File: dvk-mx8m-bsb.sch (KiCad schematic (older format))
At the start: 12 parts, among them J101 IMX8M-SOM, J102 TEST_1P

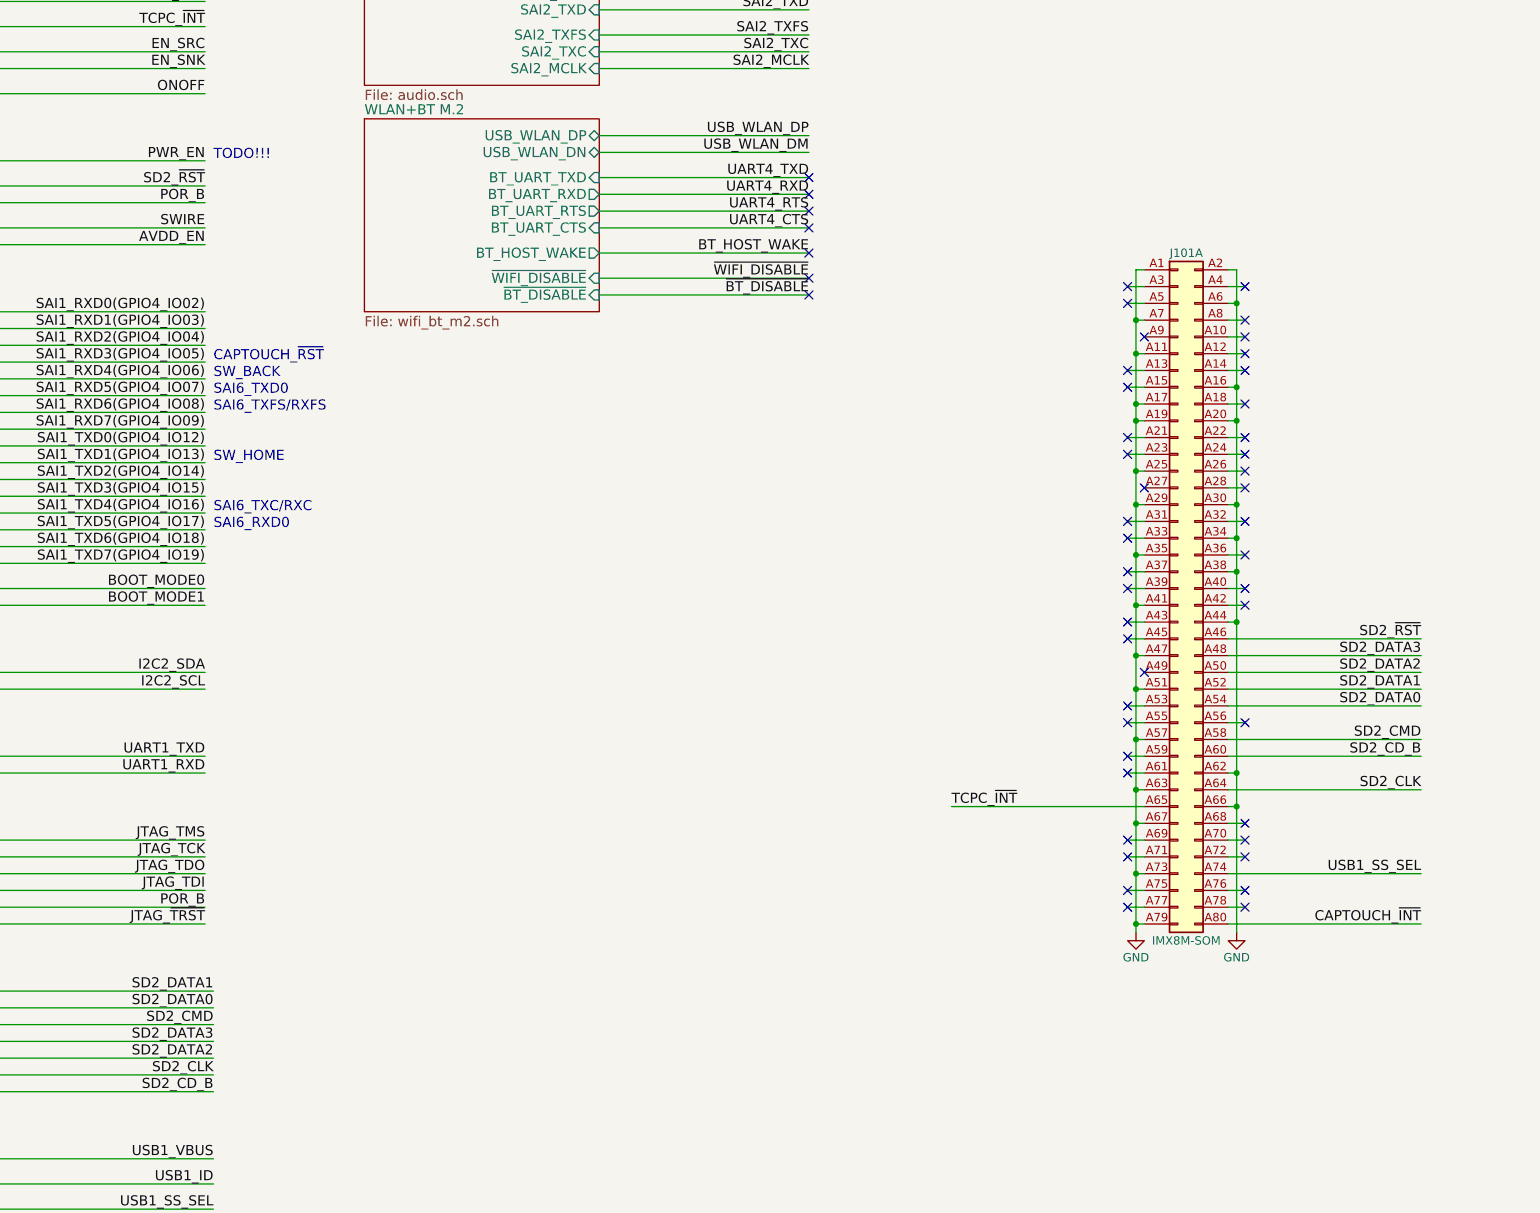
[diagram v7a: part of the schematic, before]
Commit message: Add demultiplexer to uSDHC2 for the uSD and WiFi's SDIO interfaces, include the DEMUX's (TS3A27518E) 24QFN footprint
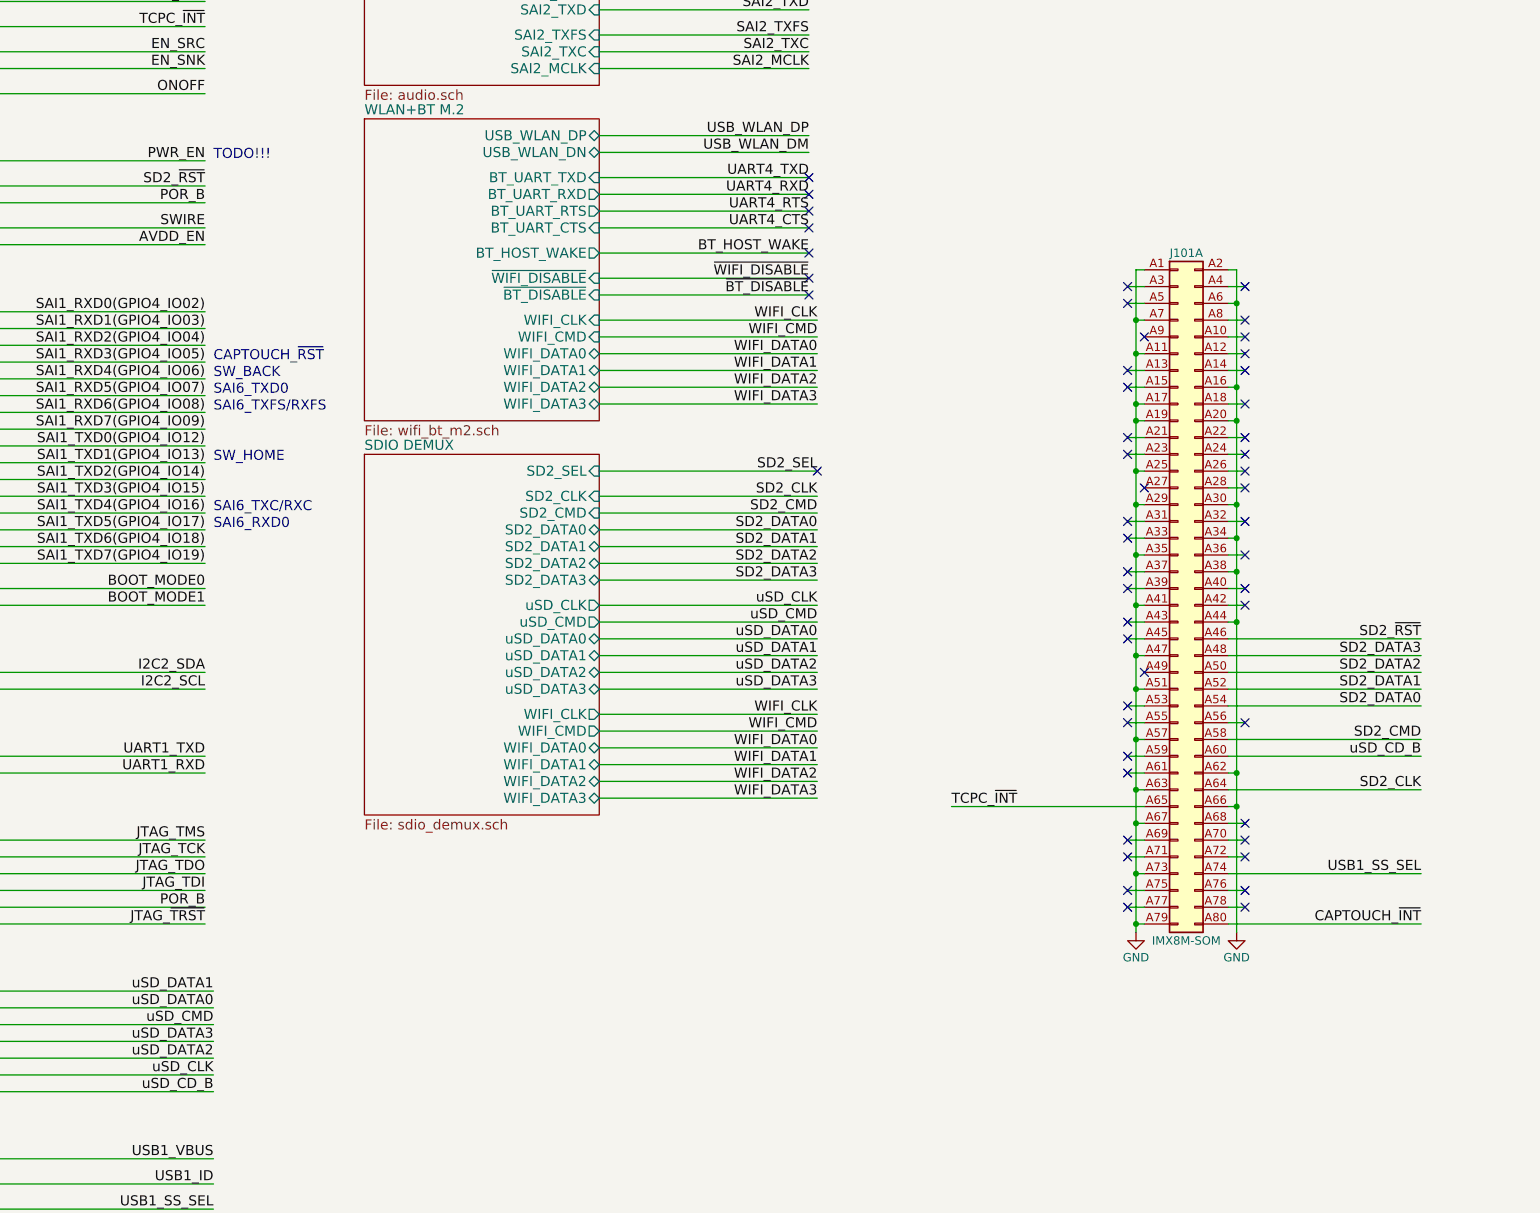
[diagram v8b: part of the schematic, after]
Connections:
- net SD2_CD_B renamed uSD_CD_B
- no-connect marks 130 -> 131
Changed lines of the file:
@@
 $Descr A2 23386 16535
 encoding utf-8
-Sheet 1 15
+Sheet 1 16
 Title "DVK-MX8M-BSB"
 Date "2018-05-02"
@@
 GPIO1_IO13
 Text Label 3250 6700 2    60   ~ 0
-SD2_DATA1
+uSD_DATA1
 Text Label 3250 6800 2    60   ~ 0
-SD2_DATA0
+uSD_DATA0
 Text Label 3250 6900 2    60   ~ 0
-SD2_CMD
+uSD_CMD
 Text Label 3250 7000 2    60   ~ 0
-SD2_DATA3
+uSD_DATA3
 Text Label 3250 7100 2    60   ~ 0
-SD2_DATA2
+uSD_DATA2
 Text Label 3250 7200 2    60   ~ 0
-SD2_CLK
+uSD_CLK
 Text Label 3250 7300 2    60   ~ 0
-SD2_CD_B
+uSD_CD_B
 Text Label 10450 4900 2    60   ~ 0
 SD2_DATA1
@@
 SD2_CLK
 Text Label 10450 5300 2    60   ~ 0
-SD2_CD_B
+uSD_CD_B
 Text Label 14200 11100 0    60   ~ 0
 UART1_RXD
@@
 USB_WWAN_DM
 $Sheet
-S 4150 1500 1400 1150
+S 4150 1500 1400 1800
 U 5AF3486B
 F0 "WLAN+BT M.2" 60
@@
 F9 "~BT_DISABLE" I R 5550 2550 60
 F10 "~WIFI_DISABLE" I R 5550 2450 60
+F11 "WIFI_CLK" I R 5550 2700 60
+F12 "WIFI_CMD" I R 5550 2800 60
+F13 "WIFI_DATA0" B R 5550 2900 60
+F14 "WIFI_DATA1" B R 5550 3000 60
+F15 "WIFI_DATA2" B R 5550 3100 60
+F16 "WIFI_DATA3" B R 5550 3200 60
 $EndSheet
 NoConn ~ 6800 1850
@@
 NoConn ~ 15250 11500
 NoConn ~ 9400 9900
+$Sheet
+S 4150 3500 1400 2150
+U 5AEA7739
+F0 "SDIO DEMUX" 60
+F1 "sdio_demux.sch" 60
+F2 "SD2_SEL" I R 5550 3600 60
+F3 "SD2_CLK" I R 5550 3750 60
+F4 "SD2_CMD" I R 5550 3850 60
+F5 "SD2_DATA0" B R 5550 3950 60
+F6 "SD2_DATA1" B R 5550 4050 60
+F7 "SD2_DATA2" B R 5550 4150 60
+F8 "SD2_DATA3" B R 5550 4250 60
+F9 "uSD_CLK" O R 5550 4400 60
+F10 "uSD_CMD" O R 5550 4500 60
+F11 "uSD_DATA0" B R 5550 4600 60
+F12 "uSD_DATA1" B R 5550 4700 60
+F13 "uSD_DATA2" B R 5550 4800 60
+F14 "uSD_DATA3" B R 5550 4900 60
+F15 "WIFI_CLK" O R 5550 5050 60
+F16 "WIFI_CMD" O R 5550 5150 60
+F17 "WIFI_DATA0" B R 5550 5250 60
+F18 "WIFI_DATA1" B R 5550 5350 60
+F19 "WIFI_DATA2" B R 5550 5450 60
+F20 "WIFI_DATA3" B R 5550 5550 60
+$EndSheet
+Text Label 6850 4050 2    60   ~ 0
+SD2_DATA1
+Text Label 6850 3950 2    60   ~ 0
+SD2_DATA0
+Text Label 6850 3850 2    60   ~ 0
+SD2_CMD
+Text Label 6850 4250 2    60   ~ 0
+SD2_DATA3
+Text Label 6850 4150 2    60   ~ 0
+SD2_DATA2
+Text Label 6850 3750 2    60   ~ 0
+SD2_CLK
+Wire Wire Line
+	5550 3750 6850 3750
+Wire Wire Line
+	5550 3850 6850 3850
+Wire Wire Line
+	5550 3950 6850 3950
+Wire Wire Line
+	5550 4050 6850 4050
+Wire Wire Line
+	5550 4150 6850 4150
+Wire Wire Line
+	5550 4250 6850 4250
+Wire Wire Line
+	5550 3600 6850 3600
+Text Label 6850 3600 2    60   ~ 0
+SD2_SEL
+Text Label 6850 4700 2    60   ~ 0
+uSD_DATA1
+Text Label 6850 4600 2    60   ~ 0
+uSD_DATA0
+Text Label 6850 4500 2    60   ~ 0
+uSD_CMD
+Text Label 6850 4900 2    60   ~ 0
+uSD_DATA3
+Text Label 6850 4800 2    60   ~ 0
+uSD_DATA2
+Text Label 6850 4400 2    60   ~ 0
+uSD_CLK
+Wire Wire Line
+	5550 4400 6850 4400
+Wire Wire Line
+	5550 4500 6850 4500
+Wire Wire Line
+	5550 4600 6850 4600
+Wire Wire Line
+	5550 4700 6850 4700
+Wire Wire Line
+	5550 4800 6850 4800
+Wire Wire Line
+	5550 4900 6850 4900
+Text Label 6850 5350 2    60   ~ 0
+WIFI_DATA1
+Text Label 6850 5250 2    60   ~ 0
+WIFI_DATA0
+Text Label 6850 5150 2    60   ~ 0
+WIFI_CMD
+Text Label 6850 5550 2    60   ~ 0
+WIFI_DATA3
+Text Label 6850 5450 2    60   ~ 0
+WIFI_DATA2
+Text Label 6850 5050 2    60   ~ 0
+WIFI_CLK
+Wire Wire Line
+	5550 5050 6850 5050
+Wire Wire Line
+	5550 5150 6850 5150
+Wire Wire Line
+	5550 5250 6850 5250
+Wire Wire Line
+	5550 5350 6850 5350
+Wire Wire Line
+	5550 5450 6850 5450
+Wire Wire Line
+	5550 5550 6850 5550
+Text Label 6850 3000 2    60   ~ 0
+WIFI_DATA1
+Text Label 6850 2900 2    60   ~ 0
+WIFI_DATA0
+Text Label 6850 2800 2    60   ~ 0
+WIFI_CMD
+Text Label 6850 3200 2    60   ~ 0
+WIFI_DATA3
+Text Label 6850 3100 2    60   ~ 0
+WIFI_DATA2
+Text Label 6850 2700 2    60   ~ 0
+WIFI_CLK
+Wire Wire Line
+	5550 2700 6850 2700
+Wire Wire Line
+	5550 2800 6850 2800
+Wire Wire Line
+	5550 2900 6850 2900
+Wire Wire Line
+	5550 3000 6850 3000
+Wire Wire Line
+	5550 3100 6850 3100
+Wire Wire Line
+	5550 3200 6850 3200
+NoConn ~ 6850 3600
 $EndSCHEMATC
